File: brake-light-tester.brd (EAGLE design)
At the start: 47.2 x 62.2 mm, 25 parts, among them J1 CON_HEADER_PRG_AVR_ICSP-SMD, SW1 TACTILE-SWITCH-7914G, U1 ATTINY85-20SU, U2 LM1117/5V, U3 TSL2561FN

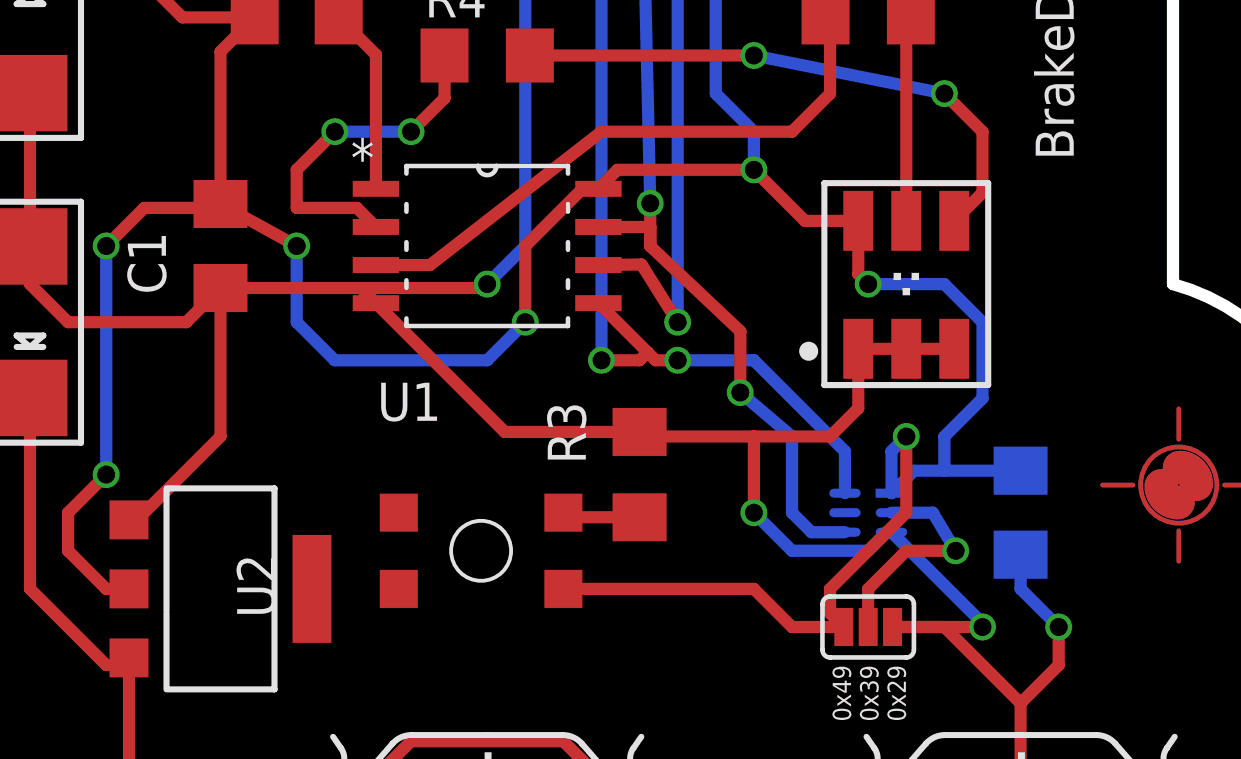
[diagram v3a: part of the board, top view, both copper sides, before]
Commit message: Now includes BOM.
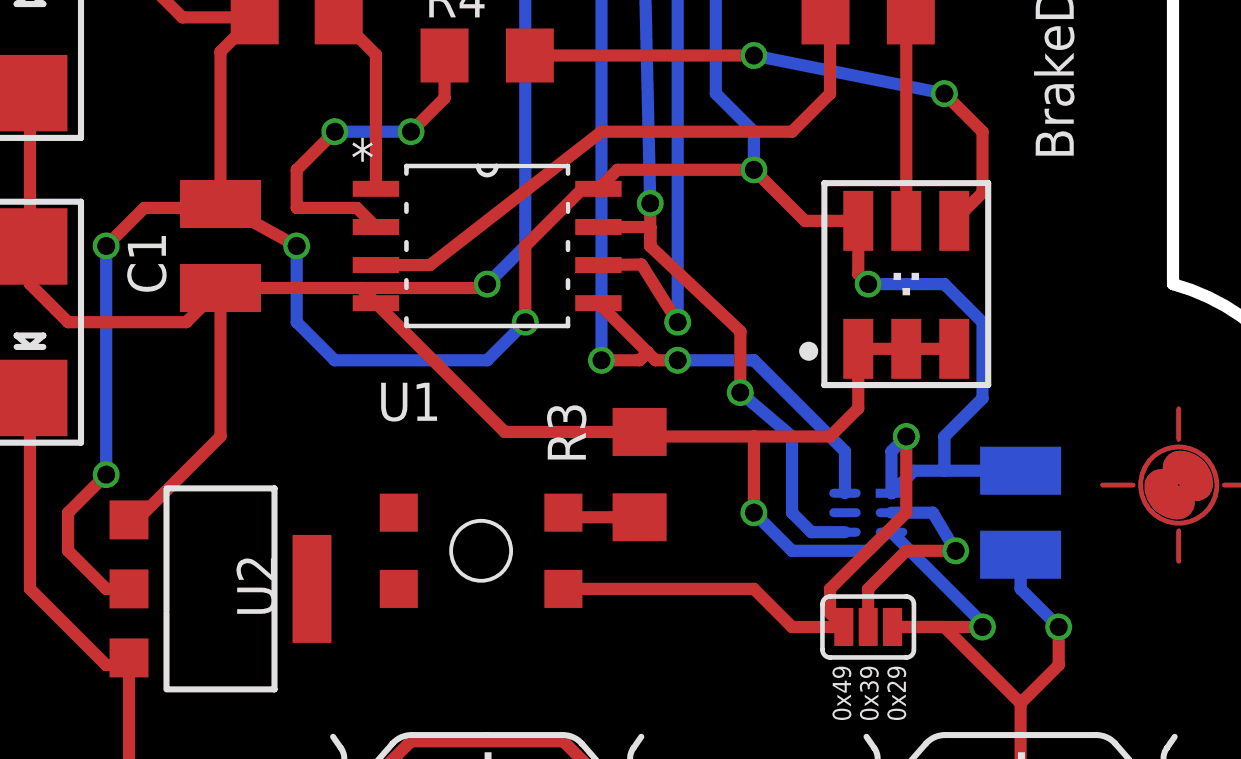
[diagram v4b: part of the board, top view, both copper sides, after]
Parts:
- C1, C5: device rcl:C1206 -> rcl:C1210
